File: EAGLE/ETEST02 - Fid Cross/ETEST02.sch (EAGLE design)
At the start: 39 parts

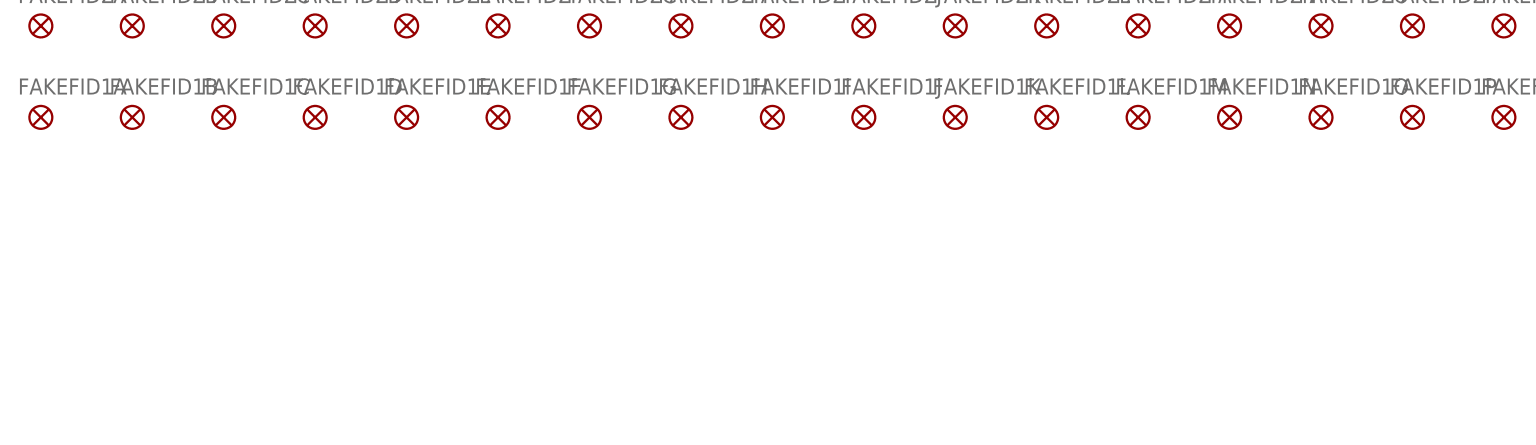
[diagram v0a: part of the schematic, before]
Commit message: Updated corners a bit, in order to squeeze in a few more fiducials.  Exported to GERBER.  Sent to board house.
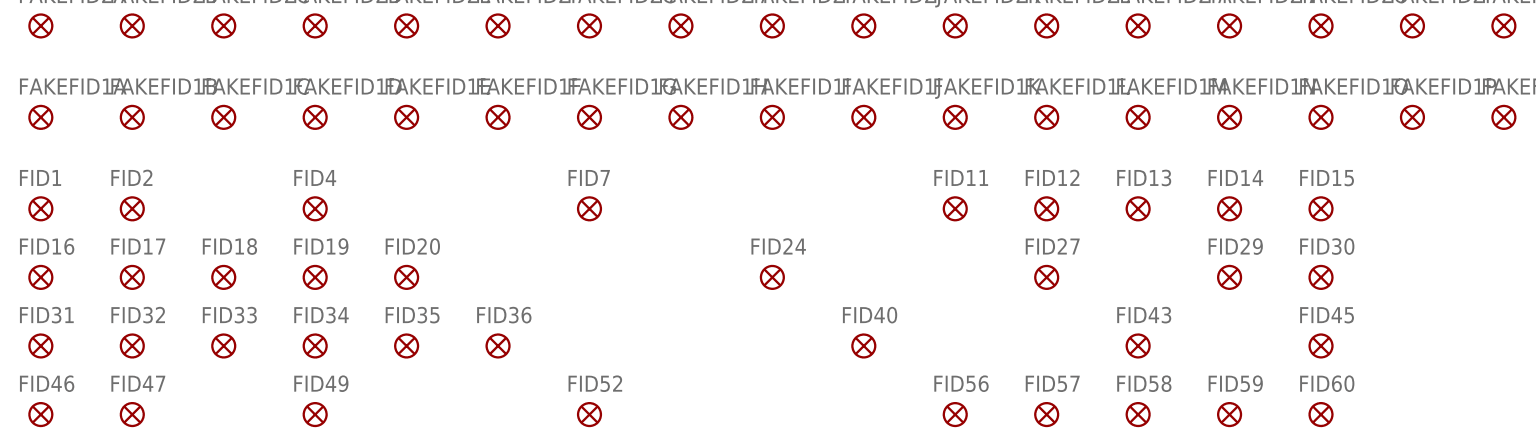
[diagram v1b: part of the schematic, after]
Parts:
- added FID1, FID11, FID12, FID13, FID14, FID15, FID16, FID17, FID18, FID19, FID2, FID20, FID24, FID27, FID29, FID30, FID31, FID32, FID33, FID34, FID35, FID36, FID4, FID40, FID43, FID45, FID46, FID47, FID49, FID52, FID56, FID57, FID58, FID59, FID60, FID7: FIDUCIAL, TinWhiskers:FIDUCIAL
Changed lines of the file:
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@@
 <setting verticaltext="up"/>
 </settings>
-<grid distance="0.1" unitdist="inch" unit="inch" style="lines" multiple="4" display="yes" altdistance="0.01" altunitdist="inch" altunit="inch"/>
+<grid distance="0.1" unitdist="inch" unit="inch" style="lines" multiple="1" display="no" altdistance="0.01" altunitdist="inch" altunit="inch"/>
 <layers>
 <layer number="1" name="Top" color="4" fill="1" visible="no" active="no"/>
@@
 <part name="FAKEFID38" library="TinWhiskers" deviceset="FIDUCIAL_19X" device=""/>
 <part name="FAKEFID39" library="TinWhiskers" deviceset="FIDUCIAL_19X" device=""/>
+<part name="FID1" library="TinWhiskers" deviceset="FIDUCIAL" device=""/>
+<part name="FID2" library="TinWhiskers" deviceset="FIDUCIAL" device=""/>
+<part name="FID4" library="TinWhiskers" deviceset="FIDUCIAL" device=""/>
+<part name="FID7" library="TinWhiskers" deviceset="FIDUCIAL" device=""/>
+<part name="FID11" library="TinWhiskers" deviceset="FIDUCIAL" device=""/>
+<part name="FID12" library="TinWhiskers" deviceset="FIDUCIAL" device=""/>
+<part name="FID13" library="TinWhiskers" deviceset="FIDUCIAL" device=""/>
+<part name="FID14" library="TinWhiskers" deviceset="FIDUCIAL" device=""/>
+<part name="FID15" library="TinWhiskers" deviceset="FIDUCIAL" device=""/>
+<part name="FID16" library="TinWhiskers" deviceset="FIDUCIAL" device=""/>
+<part name="FID17" library="TinWhiskers" deviceset="FIDUCIAL" device=""/>
+<part name="FID18" library="TinWhiskers" deviceset="FIDUCIAL" device=""/>
+<part name="FID19" library="TinWhiskers" deviceset="FIDUCIAL" device=""/>
+<part name="FID20" library="TinWhiskers" deviceset="FIDUCIAL" device=""/>
+<part name="FID24" library="TinWhiskers" deviceset="FIDUCIAL" device=""/>
+<part name="FID27" library="TinWhiskers" deviceset="FIDUCIAL" device=""/>
+<part name="FID29" library="TinWhiskers" deviceset="FIDUCIAL" device=""/>
+<part name="FID30" library="TinWhiskers" deviceset="FIDUCIAL" device=""/>
+<part name="FID31" library="TinWhiskers" deviceset="FIDUCIAL" device=""/>
+<part name="FID32" library="TinWhiskers" deviceset="FIDUCIAL" device=""/>
+<part name="FID33" library="TinWhiskers" deviceset="FIDUCIAL" device=""/>
+<part name="FID34" library="TinWhiskers" deviceset="FIDUCIAL" device=""/>
+<part name="FID35" library="TinWhiskers" deviceset="FIDUCIAL" device=""/>
+<part name="FID36" library="TinWhiskers" deviceset="FIDUCIAL" device=""/>
+<part name="FID40" library="TinWhiskers" deviceset="FIDUCIAL" device=""/>
+<part name="FID43" library="TinWhiskers" deviceset="FIDUCIAL" device=""/>
+<part name="FID45" library="TinWhiskers" deviceset="FIDUCIAL" device=""/>
+<part name="FID46" library="TinWhiskers" deviceset="FIDUCIAL" device=""/>
+<part name="FID47" library="TinWhiskers" deviceset="FIDUCIAL" device=""/>
+<part name="FID49" library="TinWhiskers" deviceset="FIDUCIAL" device=""/>
+<part name="FID52" library="TinWhiskers" deviceset="FIDUCIAL" device=""/>
+<part name="FID56" library="TinWhiskers" deviceset="FIDUCIAL" device=""/>
+<part name="FID57" library="TinWhiskers" deviceset="FIDUCIAL" device=""/>
+<part name="FID58" library="TinWhiskers" deviceset="FIDUCIAL" device=""/>
+<part name="FID59" library="TinWhiskers" deviceset="FIDUCIAL" device=""/>
+<part name="FID60" library="TinWhiskers" deviceset="FIDUCIAL" device=""/>
 </parts>
 <sheets>
@@
 <instance part="FAKEFID39" gate="R" x="375.92" y="223.52"/>
 <instance part="FAKEFID39" gate="S" x="386.08" y="223.52"/>
+<instance part="FID1" gate="G$1" x="10.16" y="30.48"/>
+<instance part="FID2" gate="G$1" x="20.32" y="30.48"/>
+<instance part="FID4" gate="G$1" x="40.64" y="30.48"/>
+<instance part="FID7" gate="G$1" x="71.12" y="30.48"/>
+<instance part="FID11" gate="G$1" x="111.76" y="30.48"/>
+<instance part="FID12" gate="G$1" x="121.92" y="30.48"/>
+<instance part="FID13" gate="G$1" x="132.08" y="30.48"/>
+<instance part="FID14" gate="G$1" x="142.24" y="30.48"/>
+<instance part="FID15" gate="G$1" x="152.4" y="30.48"/>
+<instance part="FID16" gate="G$1" x="10.16" y="22.86"/>
+<instance part="FID17" gate="G$1" x="20.32" y="22.86"/>
+<instance part="FID18" gate="G$1" x="30.48" y="22.86"/>
+<instance part="FID19" gate="G$1" x="40.64" y="22.86"/>
+<instance part="FID20" gate="G$1" x="50.8" y="22.86"/>
+<instance part="FID24" gate="G$1" x="91.44" y="22.86"/>
+<instance part="FID27" gate="G$1" x="121.92" y="22.86"/>
+<instance part="FID29" gate="G$1" x="142.24" y="22.86"/>
+<instance part="FID30" gate="G$1" x="152.4" y="22.86"/>
+<instance part="FID31" gate="G$1" x="10.16" y="15.24"/>
+<instance part="FID32" gate="G$1" x="20.32" y="15.24"/>
+<instance part="FID33" gate="G$1" x="30.48" y="15.24"/>
+<instance part="FID34" gate="G$1" x="40.64" y="15.24"/>
+<instance part="FID35" gate="G$1" x="50.8" y="15.24"/>
+<instance part="FID36" gate="G$1" x="60.96" y="15.24"/>
+<instance part="FID40" gate="G$1" x="101.6" y="15.24"/>
+<instance part="FID43" gate="G$1" x="132.08" y="15.24"/>
+<instance part="FID45" gate="G$1" x="152.4" y="15.24"/>
+<instance part="FID46" gate="G$1" x="10.16" y="7.62"/>
+<instance part="FID47" gate="G$1" x="20.32" y="7.62"/>
+<instance part="FID49" gate="G$1" x="40.64" y="7.62"/>
+<instance part="FID52" gate="G$1" x="71.12" y="7.62"/>
+<instance part="FID56" gate="G$1" x="111.76" y="7.62"/>
+<instance part="FID57" gate="G$1" x="121.92" y="7.62"/>
+<instance part="FID58" gate="G$1" x="132.08" y="7.62"/>
+<instance part="FID59" gate="G$1" x="142.24" y="7.62"/>
+<instance part="FID60" gate="G$1" x="152.4" y="7.62"/>
 </instances>
 <busses>
